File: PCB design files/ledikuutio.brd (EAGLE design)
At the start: 118.7 x 69.5 mm, 75 parts, among them IC1 ATMEGA328P, IC2 ISO7221A, IC3 74HC595D, Q2 MOSFET-NCHANNELSMD, Q3 16mhz, T1 TIP42, T2 TIP42, T3 TIP42, T4 TIP42, T5 TIP42, T6 TIP42, T7 TIP42, T8 TIP42, X1 2516-, X2 5566-20, X3 2516-, X4 2516-, X5 2516-, X6 2510-, X7 ANALOG IO

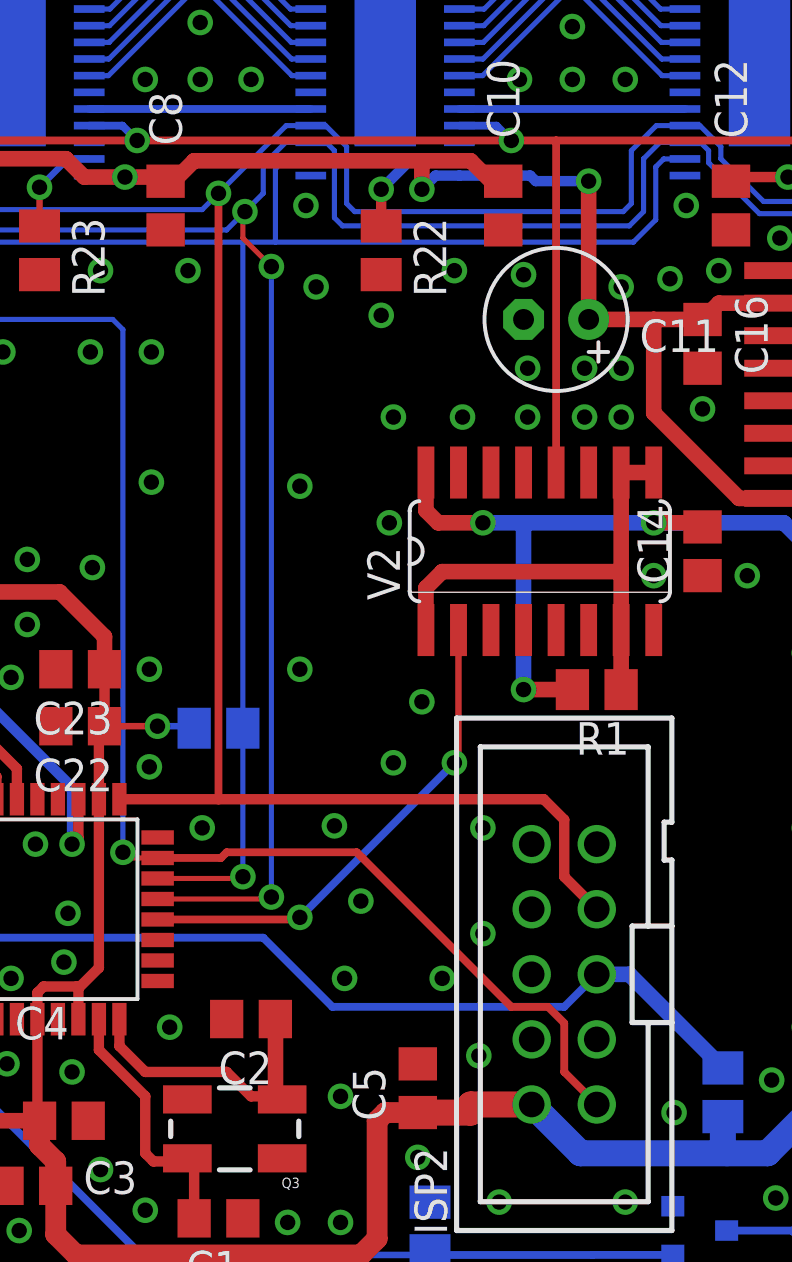
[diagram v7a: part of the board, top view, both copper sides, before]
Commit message: Connect MISO and route it. Add up-to-date gerbers and drill files.
MISO was disconnected from the MCU. (doh!). Added newest gerber files and excellon drill files. Updated the pdf files too.
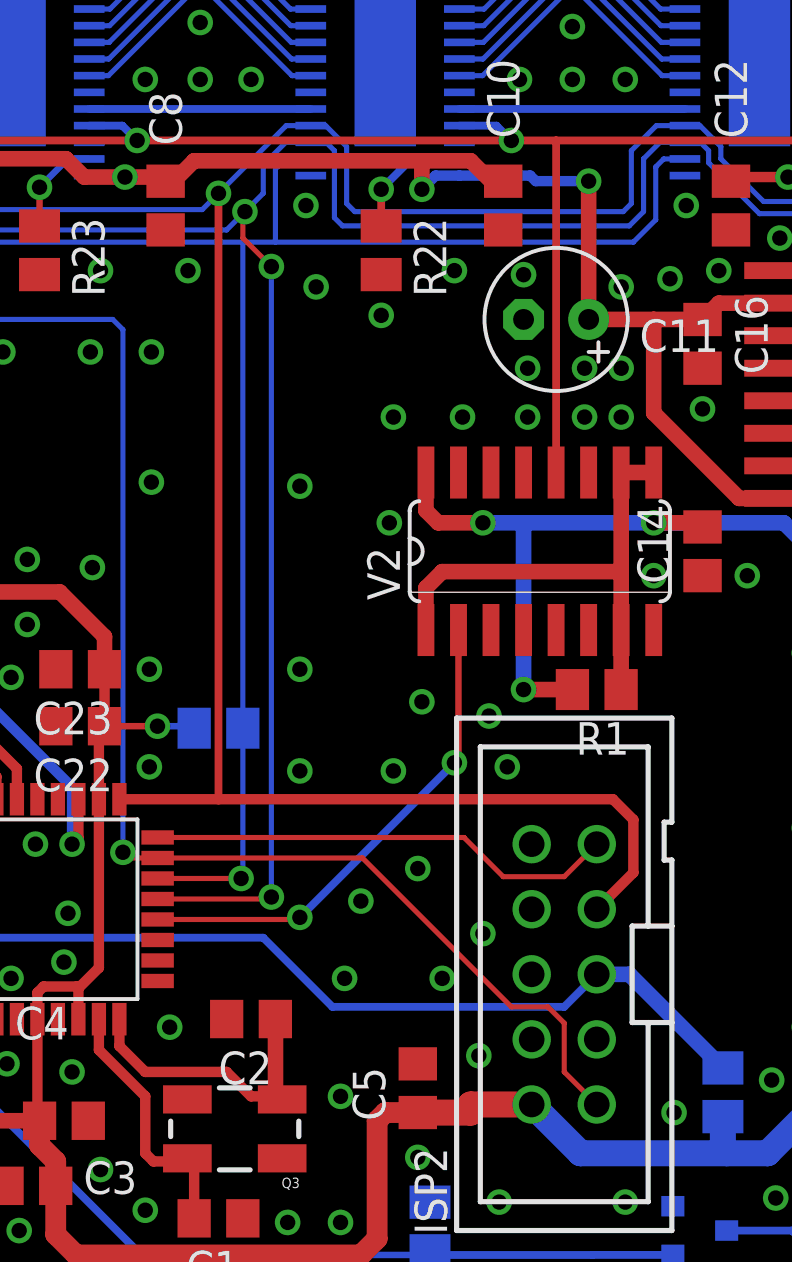
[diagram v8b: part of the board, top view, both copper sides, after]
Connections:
- net MISO: now also IC1.16
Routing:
- net MISO: track 0.00 -> 18.3 mm
- net SCLK: track 118.0 -> 120.8 mm
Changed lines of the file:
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@@
 <param name="dpMaxLengthDifference" value="10mm"/>
 <param name="dpGapFactor" value="2.5"/>
-<param name="checkGrid" value="1"/>
+<param name="checkGrid" value="0"/>
 <param name="checkAngle" value="1"/>
 <param name="checkFont" value="1"/>
@@
 <via x="54.2925" y="36.35375" extent="1-16" drill="0.6" diameter="0.8"/>
 <via x="52.07" y="36.35375" extent="1-16" drill="0.6" diameter="0.8"/>
-<via x="50.32375" y="18.415" extent="1-16" drill="0.6" diameter="0.8"/>
+<via x="51.27625" y="20.79625" extent="1-16" drill="0.6" diameter="0.8"/>
 <via x="50.32375" y="14.2875" extent="1-16" drill="0.6" diameter="0.8"/>
-<via x="44.529375" y="18.494375" extent="1-16" drill="0.6" diameter="0.8"/>
+<via x="50.561875" y="22.780625" extent="1-16" drill="0.6" diameter="0.8"/>
 <via x="27.6225" y="11.43" extent="1-16" drill="0.6" diameter="0.9"/>
 <via x="22.38375" y="9.04875" extent="1-16" drill="0.6" diameter="0.9"/>
@@
 <via x="37.385625" y="31.90875" extent="1-16" drill="0.6" diameter="0.9"/>
 <via x="37.30625" y="24.60625" extent="1-16" drill="0.6" diameter="0.9"/>
-<via x="39.37" y="18.415" extent="1-16" drill="0.6" diameter="0.8"/>
+<via x="43.18" y="20.6375" extent="1-16" drill="0.6" diameter="0.8"/>
 <via x="48.73625" y="12.54125" extent="1-16" drill="0.6" diameter="0.8"/>
 <via x="50.165" y="9.525" extent="1-16" drill="0.6" diameter="0.8"/>
@@
 <via x="43.18" y="31.75" extent="1-16" drill="0.6" diameter="0.8"/>
 <via x="43.18" y="24.60625" extent="1-16" drill="0.6" diameter="0.8"/>
-<via x="46.83125" y="20.955" extent="1-16" drill="0.6" diameter="0.8"/>
+<via x="46.83125" y="20.6375" extent="1-16" drill="0.6" diameter="0.8"/>
 <via x="47.9425" y="23.33625" extent="1-16" drill="0.6" diameter="0.8"/>
 <contactref element="X2" pad="5"/>
@@
 <via x="70.1675" y="40.16375" extent="1-16" drill="0.6" diameter="0.8"/>
 <via x="74.13625" y="40.16375" extent="1-16" drill="0.6" diameter="0.8"/>
-<wire x1="49.40585" y1="45.17225" x2="51.7525" y2="47.625" width="0" layer="19" extent="16-16"/>
+<via x="47.78375" y="16.8275" extent="1-16" drill="0.6" diameter="0.8"/>
 </signal>
 <signal name="MOSI" class="1">
@@
 <contactref element="U$1" pad="5"/>
 <contactref element="ISP2" pad="1"/>
-<wire x1="54.76875" y1="7.62" x2="53.49875" y2="8.89" width="0.3048" layer="1"/>
-<wire x1="53.49875" y1="8.89" x2="53.49875" y2="10.795" width="0.3048" layer="1"/>
-<wire x1="53.49875" y1="10.795" x2="52.86375" y2="11.43" width="0.3048" layer="1"/>
-<wire x1="52.86375" y1="11.43" x2="51.435" y2="11.43" width="0.3048" layer="1"/>
-<wire x1="51.435" y1="11.43" x2="45.625" y2="17.24" width="0.3048" layer="1"/>
+<wire x1="54.76875" y1="7.62" x2="53.49875" y2="8.89" width="0.2" layer="1"/>
+<wire x1="53.49875" y1="8.89" x2="53.49875" y2="10.795" width="0.2" layer="1"/>
+<wire x1="53.49875" y1="10.795" x2="52.86375" y2="11.43" width="0.2" layer="1"/>
+<wire x1="52.86375" y1="11.43" x2="51.435" y2="11.43" width="0.2" layer="1"/>
 <wire x1="37.6301" y1="17.24" x2="36.496875" y2="17.24" width="0.2" layer="1"/>
 <wire x1="36.496875" y1="17.24" x2="36.274375" y2="17.4625" width="0.2" layer="1"/>
@@
 <wire x1="13.0175" y1="44.45" x2="15.03965" y2="46.47215" width="0.2" layer="16"/>
 <wire x1="15.03965" y1="46.47215" x2="15.98325" y2="46.47215" width="0.2" layer="16"/>
-<wire x1="37.6301" y1="17.24" x2="40.1" y2="17.24" width="0.3048" layer="1"/>
-<wire x1="40.1" y1="17.24" x2="40.3225" y2="17.4625" width="0.3048" layer="1"/>
-<wire x1="40.3225" y1="17.4625" x2="45.4025" y2="17.4625" width="0.3048" layer="1"/>
-<wire x1="45.4025" y1="17.4625" x2="45.625" y2="17.24" width="0.3048" layer="1"/>
+<wire x1="37.6301" y1="17.24" x2="45.625" y2="17.24" width="0.2" layer="1"/>
+<wire x1="45.625" y1="17.24" x2="51.435" y2="11.43" width="0.2" layer="1"/>
 </signal>
 <signal name="GSCLK" class="1">
@@
 <wire x1="49.37125" y1="21.11375" x2="49.37125" y2="26.1366" width="0.254" layer="1"/>
 <wire x1="43.18" y1="14.9225" x2="49.2125" y2="20.955" width="0.3048" layer="16"/>
-<wire x1="37.6301" y1="14.84" x2="43.0975" y2="14.84" width="0.3048" layer="1"/>
-<wire x1="43.0975" y1="14.84" x2="43.18" y2="14.9225" width="0.3048" layer="1"/>
+<wire x1="37.6301" y1="14.84" x2="43.0975" y2="14.84" width="0.2" layer="1"/>
+<wire x1="43.0975" y1="14.84" x2="43.18" y2="14.9225" width="0.2" layer="1"/>
 <via x="43.18" y="14.9225" extent="1-16" drill="0.6"/>
 </signal>
@@
 <wire x1="42.61725" y1="44.52225" x2="42.2275" y2="44.1325" width="0.2" layer="16"/>
 <wire x1="42.2275" y1="44.1325" x2="42.2275" y2="41.275" width="0.2" layer="16"/>
-<wire x1="42.2275" y1="41.275" x2="40.9575" y2="41.275" width="0.2" layer="16"/>
+<wire x1="42.2275" y1="41.275" x2="40.955" y2="41.275" width="0.2" layer="16"/>
 <wire x1="40.955" y1="41.275" x2="27.46375" y2="41.275" width="0.2" layer="16"/>
 <wire x1="58.21075" y1="44.52225" x2="57.381" y2="44.52225" width="0.2" layer="16"/>
@@
 <wire x1="22.225" y1="40.9575" x2="14.76375" y2="40.9575" width="0.2" layer="16"/>
 <wire x1="37.6301" y1="16.44" x2="40.8875" y2="16.44" width="0.2" layer="1"/>
-<wire x1="40.8875" y1="16.44" x2="40.9575" y2="16.51" width="0.254" layer="1"/>
-<via x="40.9575" y="16.51" extent="1-16" drill="0.6"/>
 <wire x1="40.9575" y1="16.51" x2="40.9575" y2="22.301875" width="0.2" layer="16"/>
 <wire x1="40.9575" y1="22.301875" x2="40.955" y2="22.304375" width="0.2" layer="16"/>
 <wire x1="40.955" y1="22.304375" x2="40.955" y2="41.275" width="0.2" layer="16"/>
-<wire x1="40.955" y1="41.275" x2="40.9575" y2="41.275" width="0.2" layer="16"/>
+<via x="40.8875" y="16.44" extent="1-16" drill="0.6" diameter="0.8"/>
+<wire x1="40.8875" y1="16.44" x2="40.9575" y2="16.51" width="0.2" layer="16"/>
 </signal>
 <signal name="SCLK" class="1">
@@
 <wire x1="59.610625" y1="45.005625" x2="59.610625" y2="44.529375" width="0.2" layer="16"/>
 <wire x1="59.610625" y1="44.529375" x2="61.2775" y2="42.8625" width="0.2" layer="16"/>
-<wire x1="54.76875" y1="15.24" x2="53.49875" y2="16.51" width="0.4064" layer="1"/>
-<wire x1="53.49875" y1="16.51" x2="53.49875" y2="18.7325" width="0.4064" layer="1"/>
-<wire x1="53.49875" y1="18.7325" x2="52.69865" y2="19.5326" width="0.4064" layer="1"/>
-<wire x1="52.69865" y1="19.5326" x2="40.005" y2="19.5326" width="0.4064" layer="1"/>
+<wire x1="54.76875" y1="15.24" x2="56.1975" y2="16.66875" width="0.4064" layer="1"/>
+<wire x1="56.1975" y1="16.66875" x2="56.1975" y2="18.7325" width="0.4064" layer="1"/>
+<wire x1="56.1975" y1="18.7325" x2="55.3974" y2="19.5326" width="0.4064" layer="1"/>
+<wire x1="55.3974" y1="19.5326" x2="40.005" y2="19.5326" width="0.4064" layer="1"/>
 <wire x1="40.005" y1="19.5326" x2="36.1375" y2="19.5326" width="0.4064" layer="1"/>
 <wire x1="40.005" y1="19.5326" x2="40.005" y2="43.18" width="0.3048" layer="1"/>
@@
 <signal name="MISO">
 <contactref element="ISP2" pad="9"/>
+<contactref element="IC1" pad="16"/>
+<wire x1="54.76875" y1="17.78" x2="53.49875" y2="16.51" width="0.2" layer="1"/>
+<wire x1="53.49875" y1="16.51" x2="51.1175" y2="16.51" width="0.2" layer="1"/>
+<wire x1="51.1175" y1="16.51" x2="49.5875" y2="18.04" width="0.2" layer="1"/>
+<wire x1="49.5875" y1="18.04" x2="37.6301" y2="18.04" width="0.2" layer="1"/>
 </signal>
 <signal name="RESET">
@@
 <contactref element="R22" pad="1"/>
 <contactref element="U$3" pad="27"/>
-<wire x1="49.40585" y1="44.52225" x2="47.5385" y2="44.52225" width="0.4064" layer="16"/>
-<wire x1="47.5385" y1="44.52225" x2="46.355" y2="43.33875" width="0.4064" layer="16"/>
+<wire x1="49.40585" y1="44.52225" x2="47.5385" y2="44.52225" width="0.3048" layer="16"/>
+<wire x1="47.5385" y1="44.52225" x2="46.355" y2="43.33875" width="0.3048" layer="16"/>
 <via x="46.355" y="43.33875" extent="1-16" drill="0.6"/>
-<wire x1="46.355" y1="43.33875" x2="46.355" y2="41.9075" width="0.4064" layer="1"/>
+<wire x1="46.355" y1="43.33875" x2="46.355" y2="41.9075" width="0.3048" layer="1"/>
 </signal>
 </signals>
